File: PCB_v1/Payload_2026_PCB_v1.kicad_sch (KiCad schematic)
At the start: 11 parts, among them J1 SD Card Reader, J10 SW-18020P, J2 Ozone Sensor, J3 SGP40 VOC Sensor, J4 IMU, J5 BME/BMP280, J6 Ultrasonic 1, J7 Ultrasonic 2, J8 Ultrasonic 3, J9 Battery

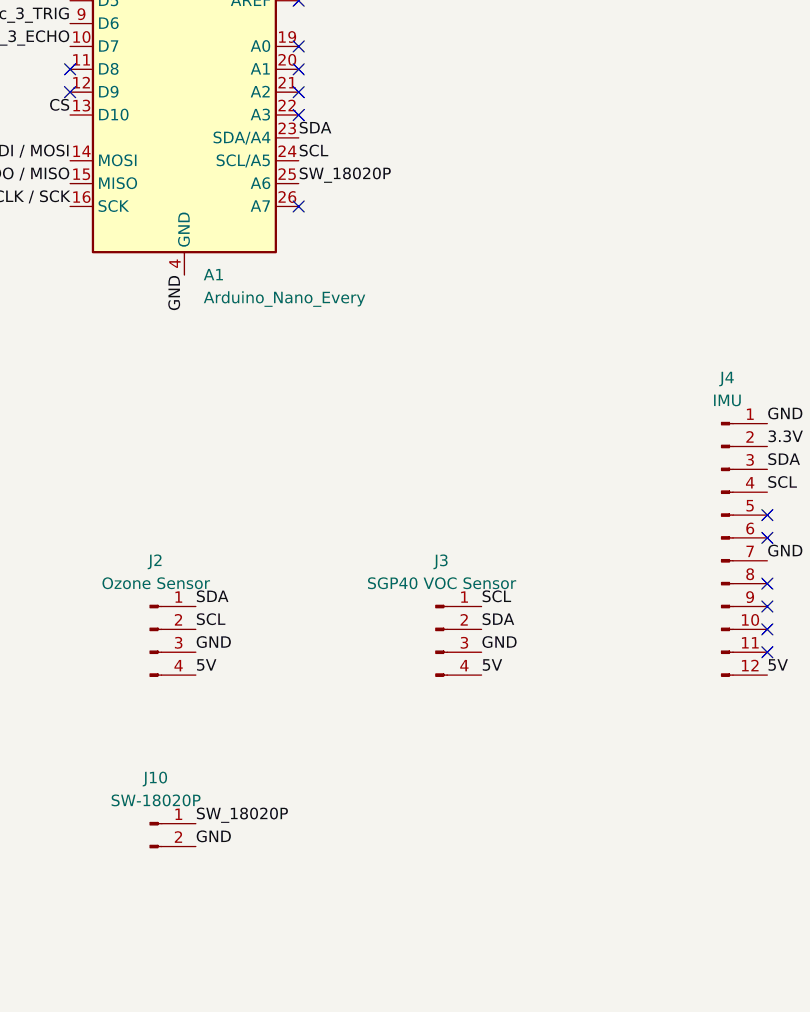
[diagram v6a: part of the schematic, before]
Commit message: Add another vibration sensor
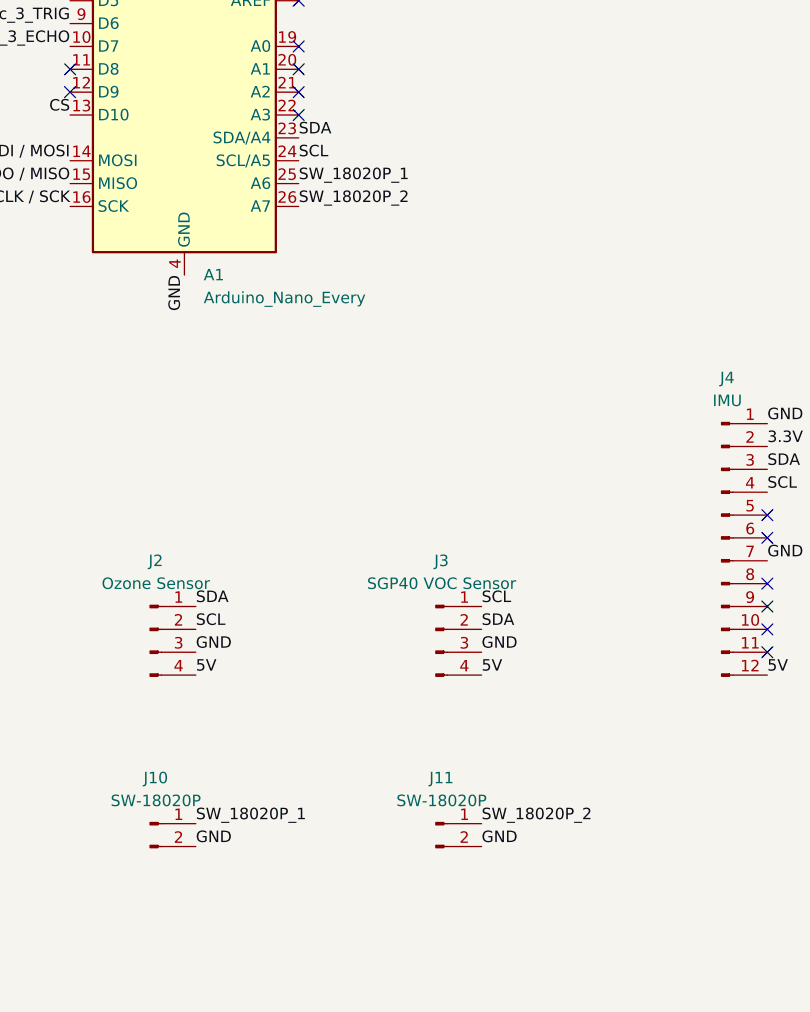
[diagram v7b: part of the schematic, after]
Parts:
- added J11: SW-18020P, Payload_2026_PCB_v1:SW_18020P, symbol Connector:Conn_01x02_Pin
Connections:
- net GND: now also J11.2 (Pin_2)
- net SW_18020P_2: now reaches A1.26 (A7)
- net SW_18020P_2: now also J11.1 (Pin_1)
- net SW_18020P renamed SW_18020P_1
- no-connect marks 20 -> 19
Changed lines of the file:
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@@
-	)
-	(no_connect
-		(at 74.93 74.93)
 	)
 	(no_connect
@@
 		)
 	)
-	(label "SW_18020P"
+	(label "SW_18020P_1"
 		(at 74.93 72.39 0)
 		(effects
@@
 		)
 	)
+	(label "SW_18020P_1"
+		(at 63.5 143.51 0)
+		(effects
+			(font
+				(size 1.27 1.27)
+			)
+			(justify left bottom)
+		)
+	)
+	(label "GND"
+		(at 95.25 146.05 0)
+		(effects
+			(font
+				(size 1.27 1.27)
+			)
+			(justify left bottom)
+		)
+	)
 	(label "GND"
 		(at 254 127 0)
@@
 		)
 	)
+	(label "SW_18020P_2"
+		(at 74.93 74.93 0)
+		(effects
+			(font
+				(size 1.27 1.27)
+			)
+			(justify left bottom)
+		)
+	)
 	(label "SCL"
 		(at 127 106.68 0)
@@
 		)
 	)
+	(label "SW_18020P_2"
+		(at 95.25 143.51 0)
+		(effects
+			(font
+				(size 1.27 1.27)
+			)
+			(justify left bottom)
+		)
+	)
 	(label "SDA"
 		(at 158.75 127 0)
@@
 	(label "GND"
 		(at 63.5 146.05 0)
-		(effects
-			(font
-				(size 1.27 1.27)
-			)
-			(justify left bottom)
-		)
-	)
-	(label "SW_18020P"
-		(at 63.5 143.51 0)
 		(effects
 			(font
@@
 					(unit 1)
 				)
+			)
+		)
+	)
+	(symbol
+		(lib_id "Connector:Conn_01x02_Pin")
+		(at 90.17 143.51 0)
+		(unit 1)
+		(exclude_from_sim no)
+		(in_bom yes)
+		(on_board yes)
+		(dnp no)
+		(fields_autoplaced yes)
+		(property "Reference" "J11"
+			(at 90.805 138.43 0)
+			(effects
+				(font
+					(size 1.27 1.27)
+				)
+			)
+		)
+		(property "Value" "SW-18020P"
+			(at 90.805 140.97 0)
+			(effects
+				(font
+					(size 1.27 1.27)
+				)
+			)
+		)
+		(property "Footprint" "Payload_2026_PCB_v1:SW_18020P"
+			(at 90.17 143.51 0)
+			(effects
+				(font
+					(size 1.27 1.27)
+				)
+				(hide yes)
+			)
+		)
+		(property "Datasheet" "~"
+			(at 90.17 143.51 0)
+			(effects
+				(font
+					(size 1.27 1.27)
+				)
+				(hide yes)
+			)
+		)
+		(property "Description" "Generic connector, single row, 01x02, script generated"
+			(at 90.17 143.51 0)
+			(effects
+				(font
+					(size 1.27 1.27)
+				)
+				(hide yes)
+			)
+		)
+		(pin "2"
+		)
+		(pin "1"
+		)
+		(instances
+			(project "Payload_2026_PCB_v1"
+				(path "/7e572a3c-507c-47f6-a212-f5f78d2e5847"
+					(reference "J11")
+					(unit 1)
+				)
